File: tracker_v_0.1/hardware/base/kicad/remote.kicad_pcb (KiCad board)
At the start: 2 copper layers, 55.4 x 97.8 mm, 26 parts, among them J15 Conn_01x09_Female, J19 Conn_01x03_Female, J2 Conn_01x12_Female, J3 Conn_01x16_Female, J4 Conn_01x06_Female, J5 Conn_01x03_Female, J6 Conn_01x05_Female, Q1 Q_NMOS_GDS, Q3 Q_NPN_EBC, SW1 SW_Push, SW2 SW_Push, SW4 SW_Push_Dual, U1 RFM95HW

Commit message: reorg
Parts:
- removed AE1: Antenna_Shield, digikey-footprints:RF_SMA_BoardEdge_142-0701-801
- removed D2: DIODE, Diode_THT:D_5W_P12.70mm_Horizontal
- removed J15: Conn_01x09_Female, Connector_PinSocket_2.54mm:PinSocket_1x09_P2.54mm_Vertical
- removed J3: Conn_01x16_Female, Connector_PinSocket_2.54mm:PinSocket_1x16_P2.54mm_Vertical
- removed J4: Conn_01x06_Female, Connector_PinSocket_2.54mm:PinSocket_1x06_P2.54mm_Vertical
- removed J6: Conn_01x05_Female, Connector_PinSocket_2.54mm:PinSocket_1x05_P2.54mm_Vertical
- removed R8: R, Resistor_THT:R_Axial_DIN0309_L9.0mm_D3.2mm_P12.70mm_Horizontal
- added D1: DIODE, Diode_THT:D_5W_P12.70mm_Horizontal, F.Cu at (10.1, 51.9)
- added J1: Conn_Coaxial, Connector_Coaxial:SMA_Amphenol_132134_Vertical, F.Cu at (-17.2, -21.0)
- added J16: Conn_01x04_Female, Connector_PinSocket_2.54mm:PinSocket_1x04_P2.54mm_Vertical, F.Cu at (-14.4, 6.93)
- added J20: Conn_01x04_Female, Connector_JST:JST_SH_SM04B-SRSS-TB_1x04-1MP_P1.00mm_Horizontal, F.Cu at (-28.3, 57.2)
- added JP1: Jumper_NO_Small, Jumper:SolderJumper-2_P1.3mm_Open_Pad1.0x1.5mm, B.Cu at (6.74, 26.3)
- added JP2: Jumper_NO_Small, Jumper:SolderJumper-2_P1.3mm_Open_Pad1.0x1.5mm, B.Cu at (-14.2, -3.46)
- added R7: R, Resistor_THT:R_Axial_DIN0309_L9.0mm_D3.2mm_P12.70mm_Horizontal, F.Cu at (4.57, 64.0)
- added SP1: SPEAKER_BUZZER5MM, Adafruit Circuit Playground:BUZZER_SMT_5MM, F.Cu at (6.82, -20.9)
- added SW3: SW_Push, Button_Switch_THT:SW_Tactile_SPST_Angled_PTS645Vx58-2LFS, F.Cu at (15.3, 9.27)
- added U2: feather, footprints:feather, F.Cu at (13.9, 46.5)
- added U3: Adafruit_IMU_BNO005, footprints:IMU_Ada_BNO005, F.Cu at (-23.7, 1.96)
- added U4: Adafruit_Sharp_Display_1_3, footprints:Display_adafruit_sharp_13, F.Cu at (0.00, 41.9)
- added U5: neo-6m-black, footprints:gps_neo6m_black, F.Cu at (-15.2, 35.6)
- J2: value Conn_01x12_Female -> Conn_01x06_Female; footprint Connector_PinSocket_2.54mm:PinSocket_1x12_P2.54mm_Vertical -> Connector_PinHeader_2.54mm:PinHeader_1x06_P2.54mm_Vertical
- Q1: footprint Package_TO_SOT_THT:TO-220-3_Vertical -> Package_TO_SOT_THT:TO-220-3_Horizontal_TabUp
- R3: value 4.7K -> 10K
- R5: value R -> 4.7K
- R6: value 10K -> 4.7K
- moved Q3 123.4 mm to (-26.9, 36.6), turned to 90 degrees
- moved J2 118.9 mm to (-26.1, 14.9), turned to 0 degrees
- moved R1 118.5 mm to (-19.8, 51.3), turned to 270 degrees
- moved SW1 117.0 mm to (15.2, -15.3)
- moved SW2 113.8 mm to (15.3, -0.69)
- moved SW4 113.5 mm to (-12.9, 74.6), turned to 180 degrees
- moved R2 113.1 mm to (-15.7, 51.3), turned to 270 degrees
- moved Q1 112.8 mm to (7.53, 3.15), turned to 180 degrees
- moved U1 110.5 mm to (-1.71, -1.35)
- moved J5 109.5 mm to (19.7, 28.6), turned to 0 degrees
- moved R3 102.2 mm to (-11.7, 64.0), turned to 90 degrees
- moved R5 100.7 mm to (-3.55, 64.0), turned to 90 degrees
- moved J19 97.5 mm to (-1.54, 73.8), turned to 270 degrees
- moved H5 97.0 mm to (17.8, -21.8)
- moved H6 96.1 mm to (-28.1, -21.8)
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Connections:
- net ~{RESET} renamed ~RESET
- H1 pad 1: unconnected-(H1-Pad1) -> GND
- J19 pad 1: unconnected-(J19-Pad1) -> (no net)
- J19 pad 2: Net-(J19-Pad2) -> GND
- J19 pad 3: A3 -> A5
- J2 pad 1: VBAT -> GND
- J2 pad 2: EN -> D10
- J2 pad 3: VBUS -> D13
- J2 pad 4: D13 -> A1
- J2 pad 5: D12 -> A0
- J2 pad 6: D11 -> +3V3
- J5 pad 1: GND -> (no net)
- J5 pad 2: VBAT -> EN
- J5 pad 3: VBAT_EXT -> GND
- R3 pad 1: +3V3 -> D9
- R3 pad 2: A5 -> GND
- R5 pad 1: Net-(J19-Pad2) -> +3V3
- R5 pad 2: GND -> A3
- R6 pad 1: D9 -> +3V3
- R6 pad 2: GND -> A2
- SW1 pad 1: A4 -> A2
- SW2 pad 1: A5 -> A3
- U1 pad 1: unconnected-(U1-Pad1) -> GND
- U1 pad 10: unconnected-(U1-Pad10) -> GND
- U1 pad 11: unconnected-(U1-Pad11) -> (no net)
- U1 pad 12: unconnected-(U1-Pad12) -> (no net)
- U1 pad 13: unconnected-(U1-Pad13) -> +3V3
- U1 pad 14: unconnected-(U1-Pad14) -> D12
- U1 pad 15: unconnected-(U1-Pad15) -> Net-(JP2-Pad1)
- U1 pad 16: unconnected-(U1-Pad16) -> (no net)
- U1 pad 2: unconnected-(U1-Pad2) -> MISO
- U1 pad 3: unconnected-(U1-Pad3) -> MOSI
- U1 pad 4: unconnected-(U1-Pad4) -> SCK
- U1 pad 5: unconnected-(U1-Pad5) -> D11
- U1 pad 6: unconnected-(U1-Pad6) -> D6
- U1 pad 7: unconnected-(U1-Pad7) -> (no net)
- U1 pad 8: unconnected-(U1-Pad8) -> GND
- U1 pad 9: unconnected-(U1-Pad9) -> Net-(J1-Pad1)
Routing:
- net GND: track 0.00 -> 408.4 mm, vias 0 -> 24
- net +3V3: track 0.00 -> 270.7 mm, vias 0 -> 18
- net SDA: track 0.00 -> 189.5 mm, vias 0 -> 11
- net Net-(D1-Pad2): track 0.00 -> 173.8 mm, vias 0 -> 10
- net SCL: track 0.00 -> 141.8 mm, vias 0 -> 9
- net D10: track 0.00 -> 119.4 mm, vias 0 -> 4
- net D13: track 0.00 -> 118.1 mm, vias 0 -> 5
- net D6: track 0.00 -> 105.8 mm, vias 0 -> 5
- net D9: track 0.00 -> 91.8 mm, vias 0 -> 6
- net D12: track 0.00 -> 90.7 mm, vias 0 -> 3
- net D11: track 0.00 -> 89.1 mm, vias 0 -> 5
- net A1: track 0.00 -> 85.6 mm, vias 0 -> 3
- net A2: track 0.00 -> 84.0 mm, vias 0 -> 5
- net A0: track 0.00 -> 80.1 mm, vias 0 -> 2
- net SCK: track 0.00 -> 78.0 mm, vias 0 -> 5
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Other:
- board size 55.4 x 97.8 mm -> 53.3 x 115.3 mm
- net class Default added: clearance 0.2, trace_width 0.25, via_dia 0.8, via_drill 0.4
- board text added: "3.7V"
- board text added: "3V3"
- board text added: "A"
- board text added: "A1"
- board text added: "ANT"
- board text added: "ANTENNA"
- board text added: "B"
- board text added: "C"
- board text added: "D11"
- board text added: "D12"
- board text added: "D13"
- board text added: "G1"
- board text added: "GND"
- board text added: "JST"
- board text added: "LOG"
- board text added: "OFF"
- board text added: "ON"
- board text added: "RESET"
- board text added: "RFM95"
- board text added: "RX_DO"
- board text added: "SCL"
- board text added: "Sharp display"
- board text added: "Sharp display breakout"
- board text added: "TX_D1"
- board text added: "pvos.org/tracker"
- board text added: "tracker"
- board text added: "tracker v0.1"
- board text added: "v0.1"
- board text removed: "100"
- board text removed: "10K"
- board text removed: "4.7K"
- board text removed: "Feather_1"
- board text removed: "Sharp Display"

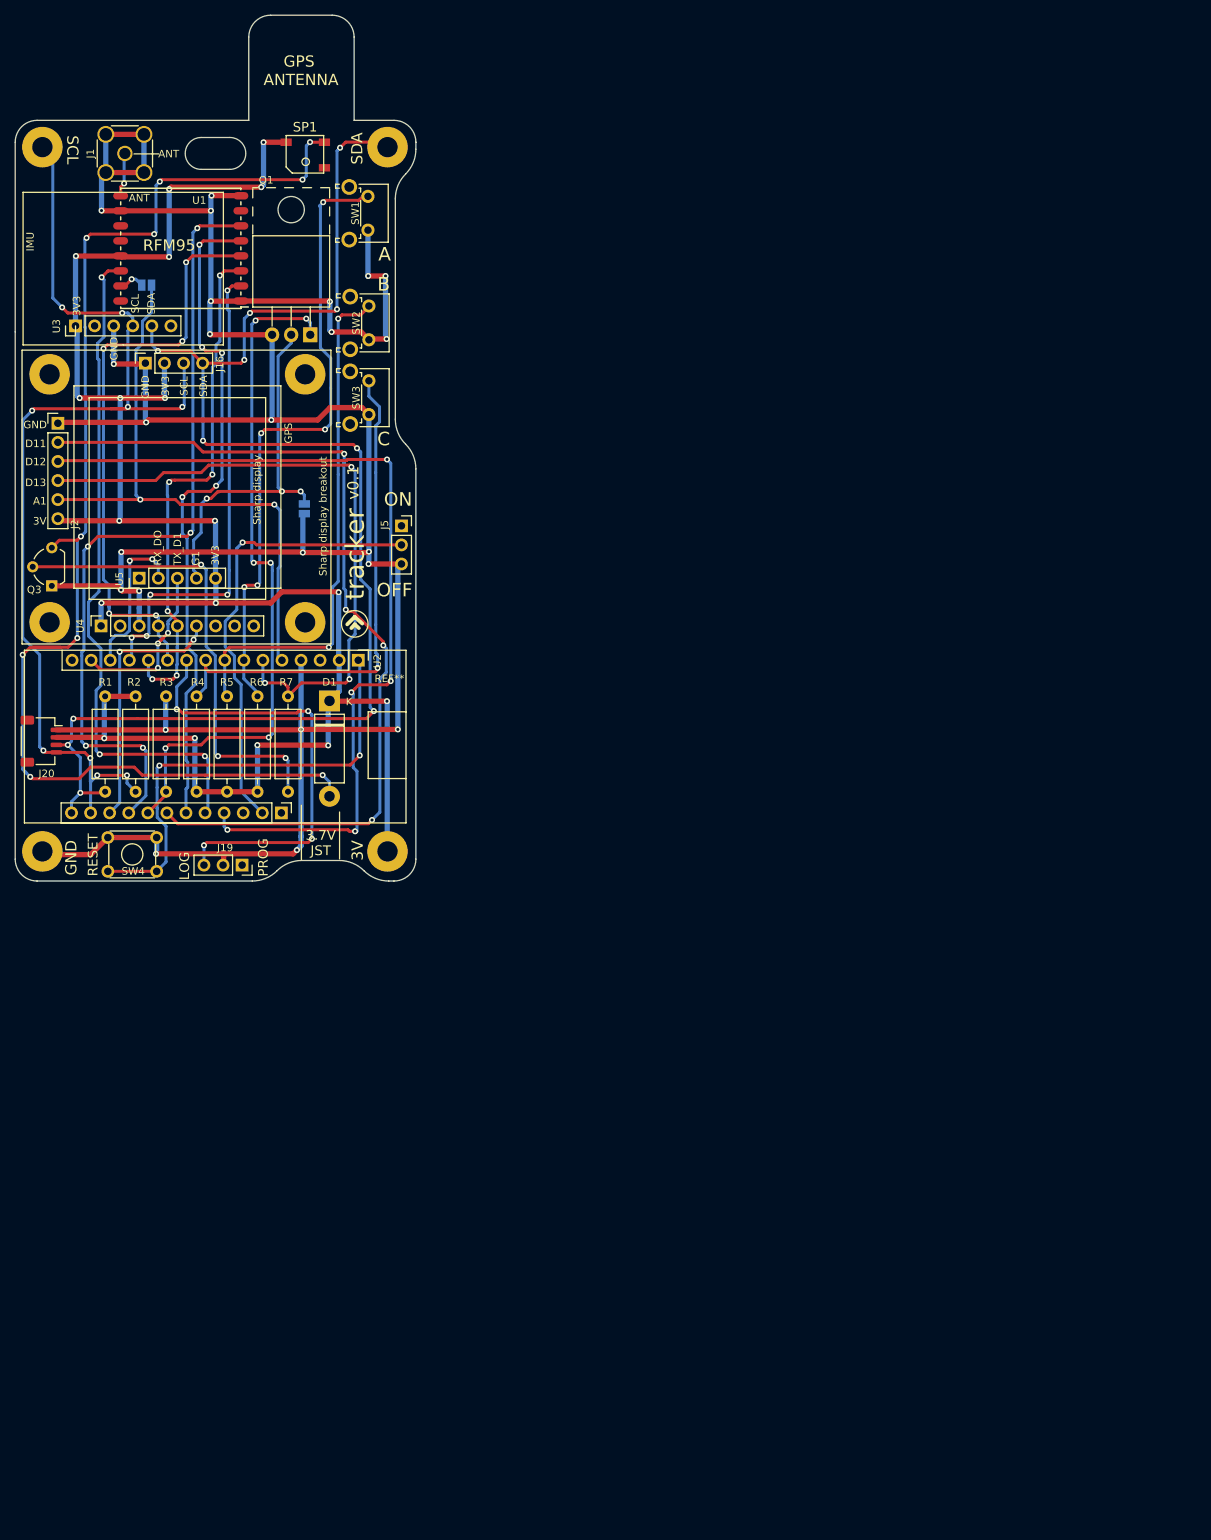
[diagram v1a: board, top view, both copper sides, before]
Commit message: node repackaging
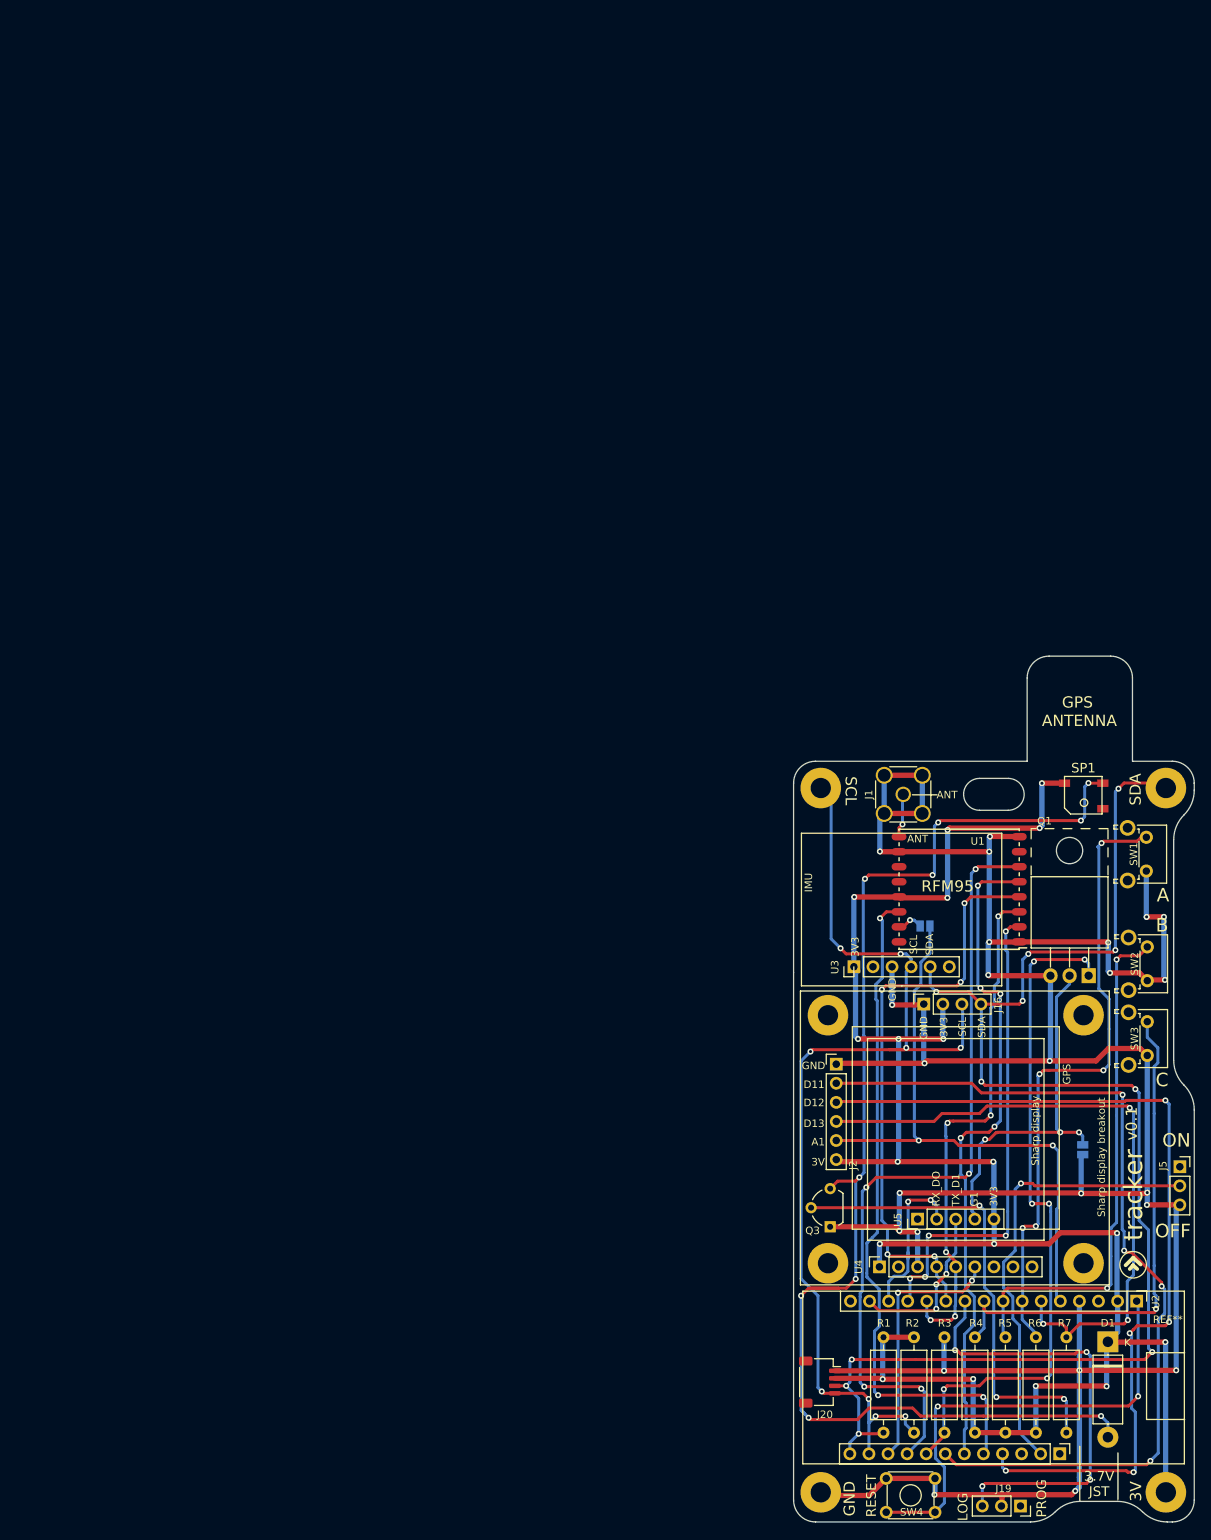
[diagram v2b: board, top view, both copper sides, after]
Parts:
- moved D1 134.2 mm to (113.7, 137.2)
- moved H1 134.2 mm to (75.5, 157.2)
- moved H2 134.2 mm to (121.4, 157.2)
- moved H5 134.2 mm to (121.4, 63.5)
- moved H6 134.2 mm to (75.5, 63.5)
- moved J1 134.2 mm to (86.5, 64.3)
- moved J16 134.2 mm to (89.2, 92.3)
- moved J19 134.2 mm to (102.1, 159.1)
- moved J2 134.2 mm to (77.6, 100.3)
- moved J20 134.2 mm to (75.4, 142.6)
- moved J5 134.2 mm to (123.3, 113.9)
- moved JP1 134.2 mm to (110.4, 111.6)
- moved JP2 134.2 mm to (89.4, 81.9)
- moved Q1 134.2 mm to (111.2, 88.5)
- moved Q3 134.2 mm to (76.7, 121.9)
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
